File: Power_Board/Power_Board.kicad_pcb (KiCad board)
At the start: 2 copper layers, 70.6 x 70.4 mm, 20 parts, among them J1 Conn_01x10_Female, J2 Conn_01x10_Female, J3 Conn_01x06_Female, J4 Screw_Terminal_01x02, J5 Screw_Terminal_01x02

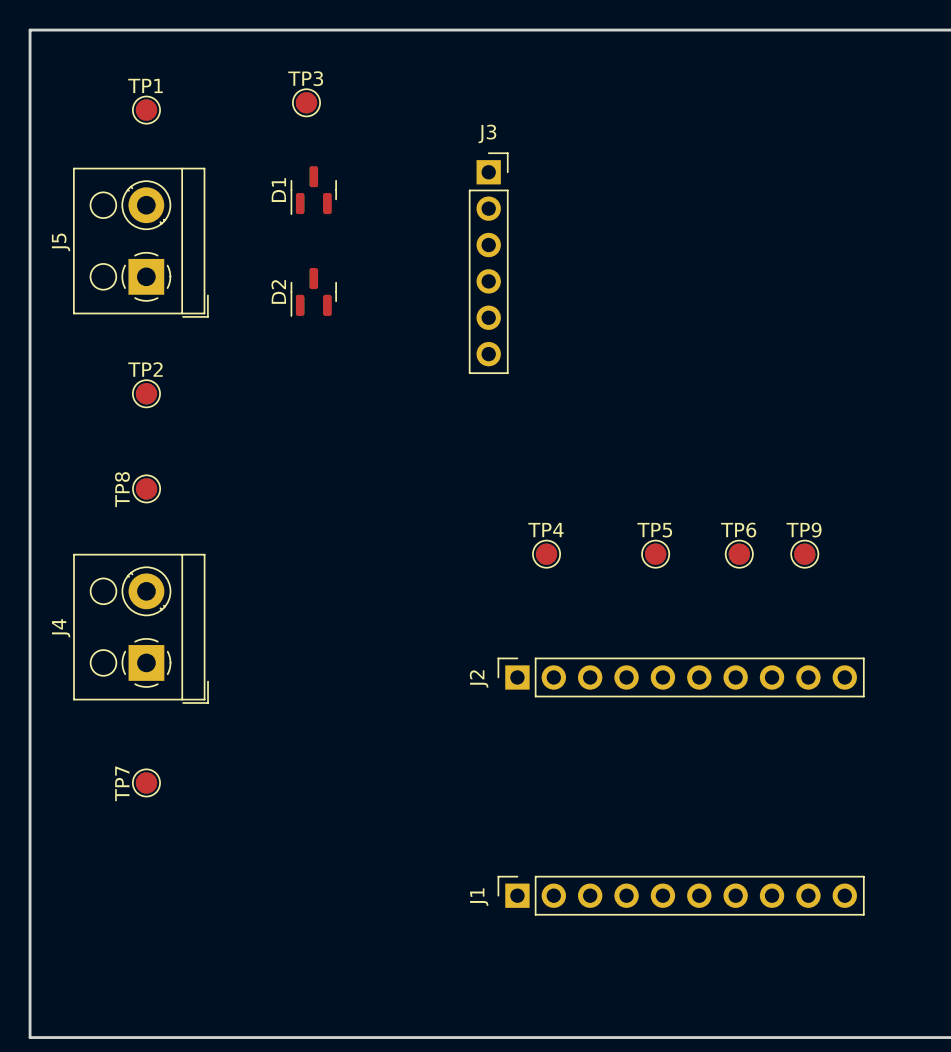
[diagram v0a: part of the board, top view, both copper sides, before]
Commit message: Removed sensor from board
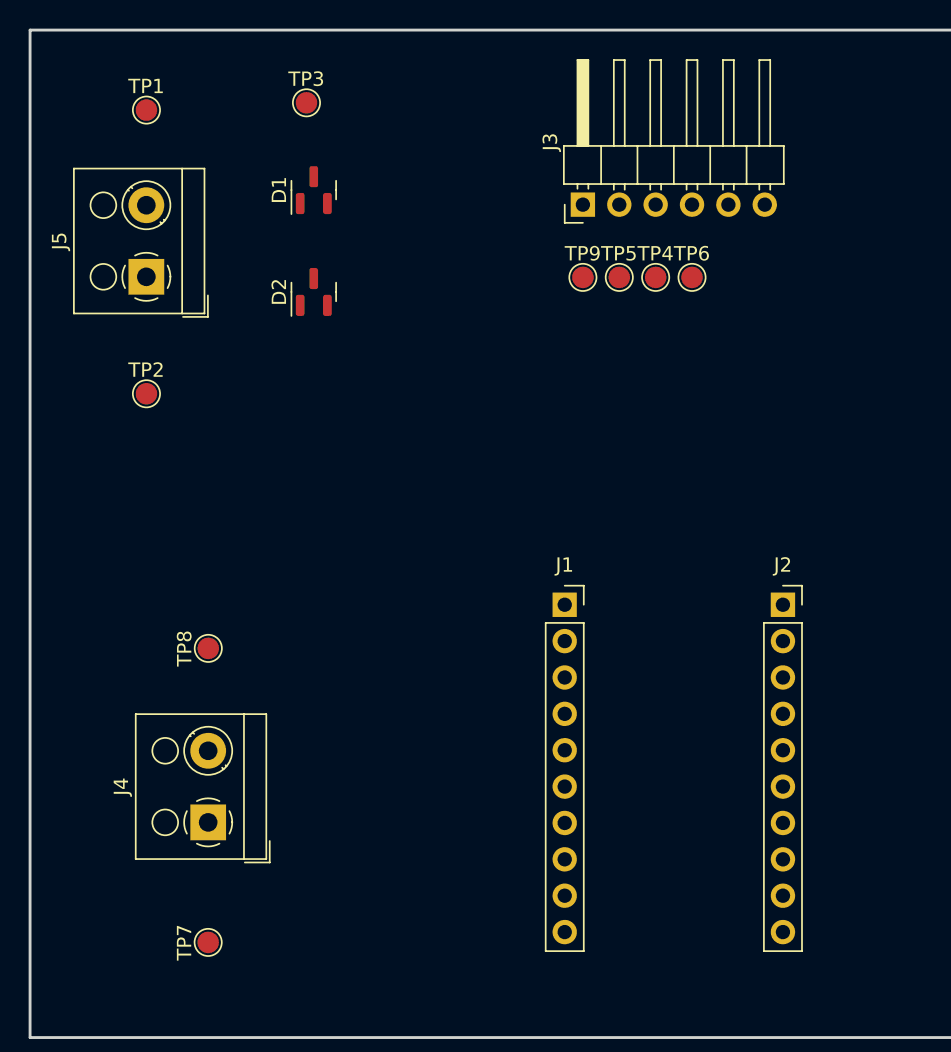
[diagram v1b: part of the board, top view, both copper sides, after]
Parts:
- J3: value Conn_01x06_Female -> Conn_01x06_Male; footprint Connector_PinSocket_2.54mm:PinSocket_1x06_P2.54mm_Vertical -> Connector_PinHeader_2.54mm:PinHeader_1x06_P2.54mm_Horizontal
- TP4: value VDDOUT -> SDA
- TP5: value 1.15 -> VDDOUT
- TP6: value 1.13 -> SCL
- moved TP9 24.8 mm to (138.4, 38.1)
- moved TP4 20.8 mm to (143.5, 38.1)
- moved J1 20.6 mm to (137.2, 61.0), turned to 0 degrees
- moved TP6 19.6 mm to (146.1, 38.1)
- moved TP5 19.5 mm to (141.0, 38.1)
- moved J2 19.2 mm to (152.4, 61.0), turned to 0 degrees
- moved J4 11.9 mm to (112.3, 76.2)
- moved TP7 11.9 mm to (112.3, 84.5)
- moved TP8 11.9 mm to (112.3, 64.0)
- moved J3 6.96 mm to (138.4, 33.0), turned to 90 degrees
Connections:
- J1 pad 1: 0.13 -> SCL
- J2 pad 2: 3V3 -> VDDOUT
- J3 pad 2: 3V3 -> VDDOUT
- J3 pad 3: 1.15 -> 0.15
- J3 pad 4: 1.13 -> SCL
- TP4 pad 1: 3V3 -> 0.15
- TP5 pad 1: 1.15 -> VDDOUT
- TP6 pad 1: 1.13 -> SCL

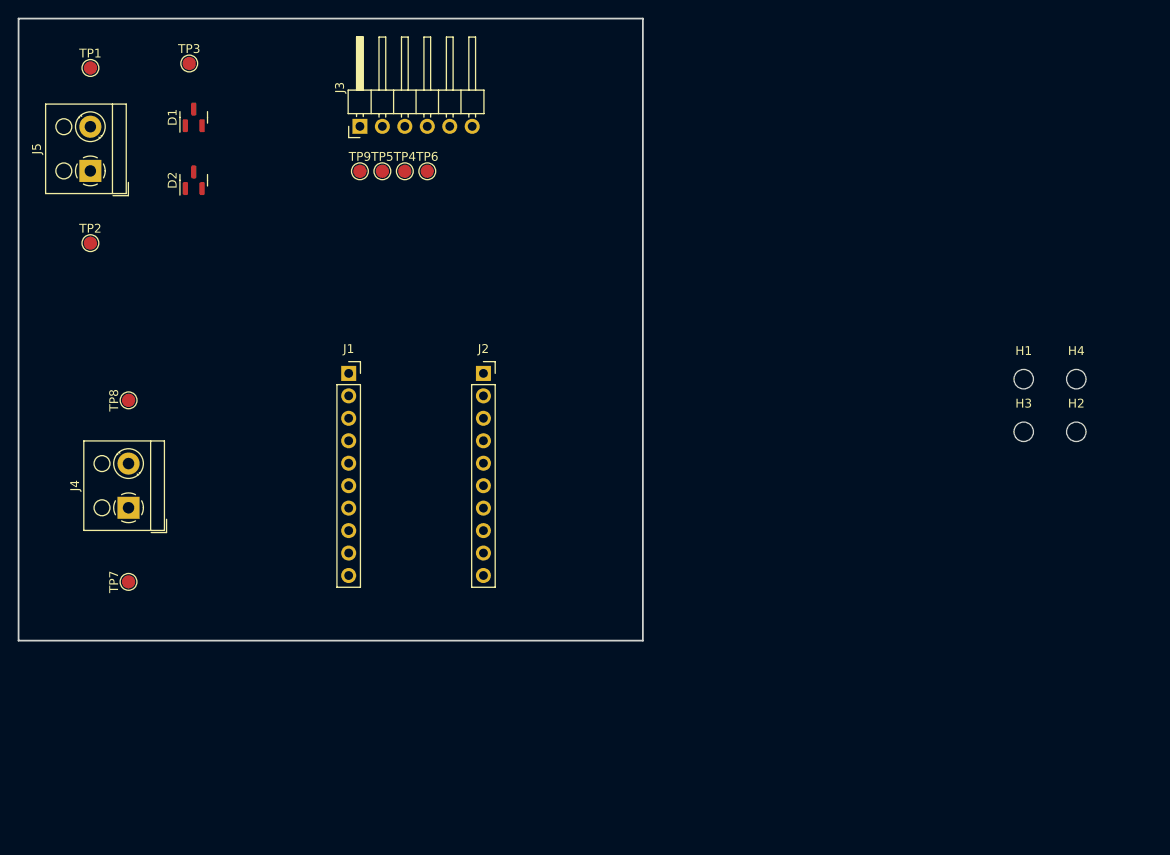
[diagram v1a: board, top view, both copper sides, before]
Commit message: new pcb layout
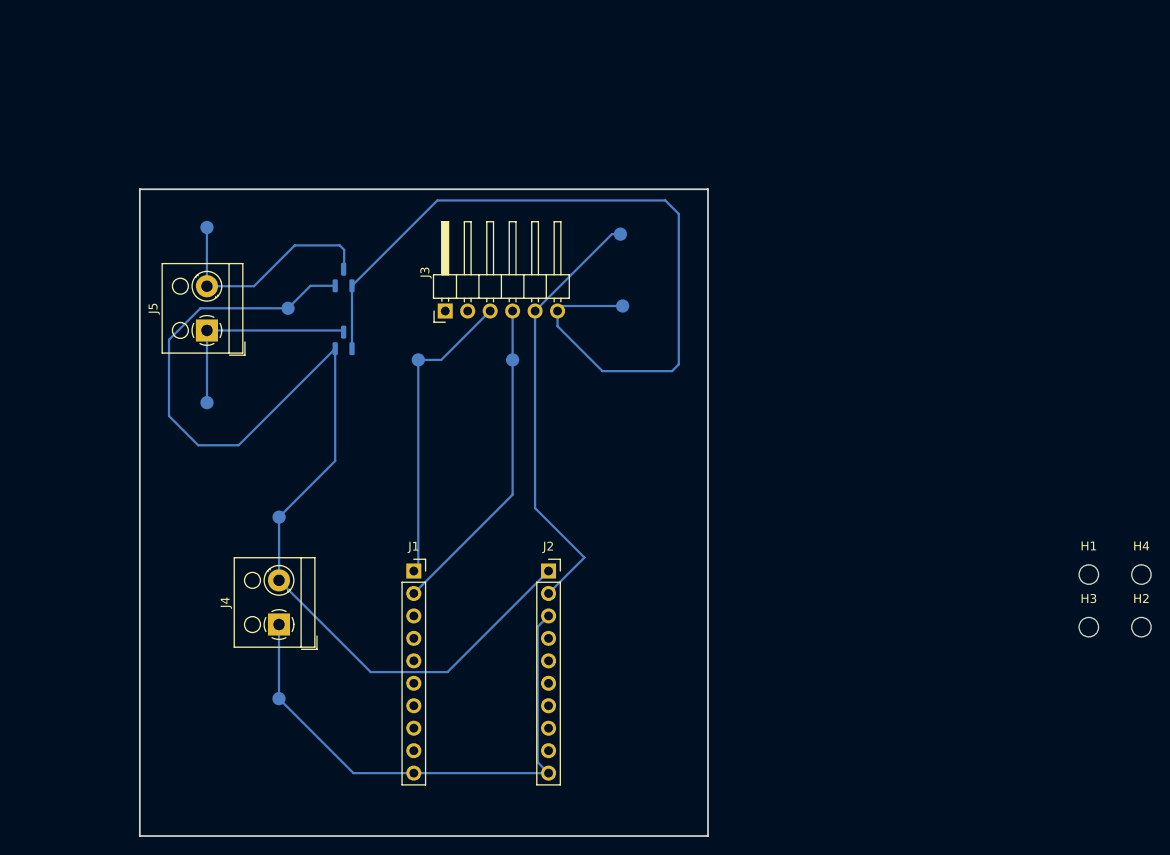
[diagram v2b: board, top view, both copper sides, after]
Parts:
- D1, D2, TP1, TP2, TP3, TP4, TP5, TP6, TP7, TP8, TP9: moved to B.Cu
- moved TP9 33.4 mm to (168.1, 53.3), turned to 180 degrees
- moved TP3 29.9 mm to (130.3, 53.6), turned to 180 degrees
- moved TP5 27.8 mm to (167.9, 45.2), turned to 180 degrees
- moved D1 24.8 mm to (136.6, 50.1)
- moved D2 24.8 mm to (136.6, 57.2)
- moved TP4 24.6 mm to (155.7, 59.4), turned to 180 degrees
- moved J1 23.5 mm to (144.5, 83.3)
- moved J2 23.5 mm to (159.8, 83.3)
- moved H2 23.3 mm to (226.8, 89.7)
- moved H3 23.3 mm to (220.9, 89.7)
- moved H1 23.3 mm to (220.9, 83.7)
- moved H4 23.3 mm to (226.8, 83.7)
- moved J3 23.0 mm to (148.1, 53.9)
- moved J5 22.3 mm to (121.1, 56.1)
- moved TP1 22.3 mm to (121.1, 44.5), turned to 180 degrees
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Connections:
- J1 pad 1: SCL -> 0.13
- J2 pad 2: VDDOUT -> 3V3
- J3 pad 1: GND -> 1V8
- J3 pad 2: VDDOUT -> INT
- J3 pad 3: 0.15 -> 0.13
- J3 pad 4: SCL -> 0.15
- J3 pad 5: INT -> 3V3
- J3 pad 6: 1V8 -> GND
- TP5 pad 1: VDDOUT -> 3V3
- TP6 pad 1: SCL -> 0.13
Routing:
- net GND: track 0.00 -> 152.3 mm
- net VBUS: track 0.00 -> 123.0 mm
- net 3V3: track 0.00 -> 49.2 mm
- net 0.15: track 0.00 -> 36.6 mm
- net 0.13: track 0.00 -> 34.5 mm
- net Net-(D1-Pad3): track 0.00 -> 26.5 mm
- net Net-(D2-Pad3): track 0.00 -> 23.7 mm
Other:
- board size 70.6 x 70.4 mm -> 64.3 x 73.2 mm

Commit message: Added GND plane and rerouted
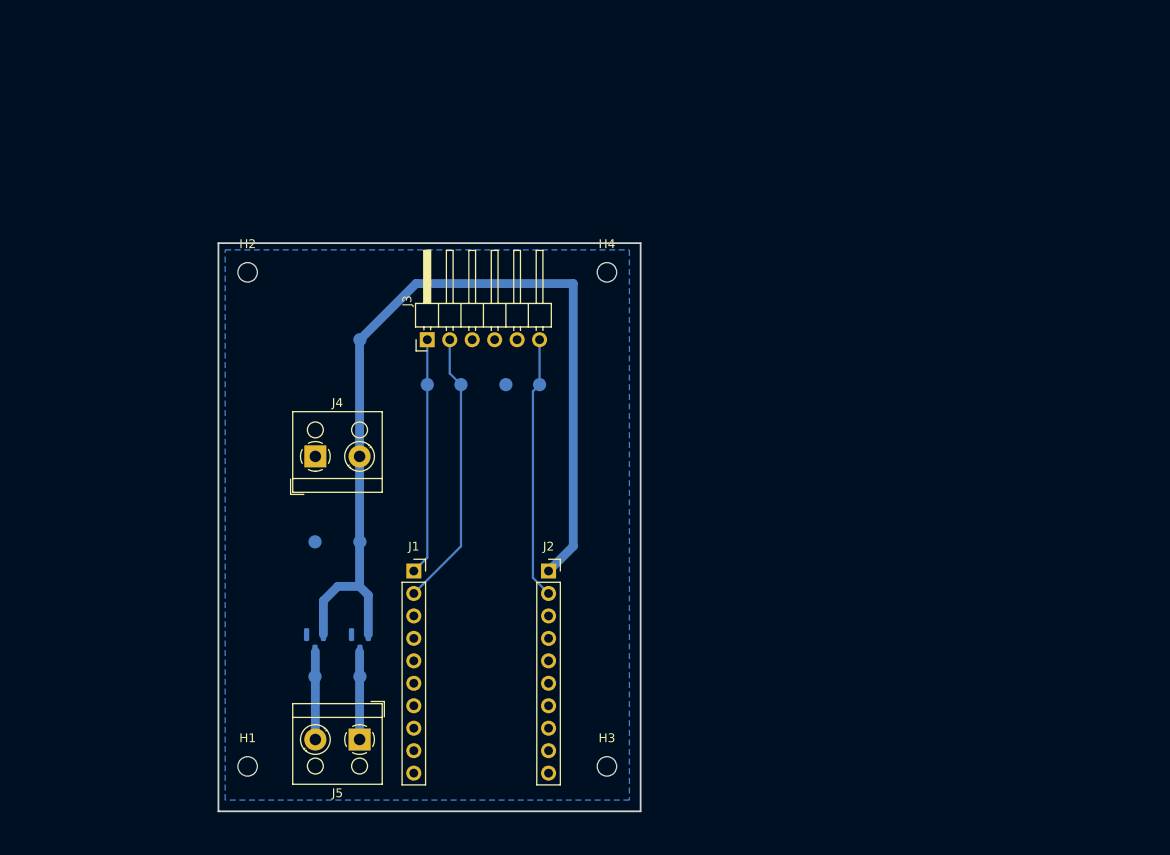
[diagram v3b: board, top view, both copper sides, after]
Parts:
- moved H2 108.8 mm to (125.7, 49.5)
- moved H1 97.6 mm to (125.7, 105.4)
- moved H4 69.4 mm to (166.4, 49.5)
- moved H3 56.7 mm to (166.4, 105.4)
- moved TP1 52.2 mm to (133.3, 95.2)
- moved J5 49.4 mm to (138.4, 102.4), turned to 180 degrees
- moved D1 41.5 mm to (133.3, 91.4), turned to -90 degrees
- moved TP2 35.5 mm to (138.4, 95.2)
- moved D2 34.3 mm to (138.4, 91.4), turned to -90 degrees
- moved TP3 27.6 mm to (138.4, 80.0)
- moved TP8 22.1 mm to (138.4, 57.1)
- moved J4 19.5 mm to (133.4, 70.3), turned to 0 degrees
- moved TP5 19.3 mm to (158.8, 62.2)
- moved TP7 18.2 mm to (133.3, 80.0)
- moved TP9 15.9 mm to (154.9, 62.2)
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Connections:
- J2 pad 2: 3V3 -> VDDOUT
- J3 pad 1: 1V8 -> 0.13
- J3 pad 2: INT -> 0.15
- J3 pad 3: 0.13 -> INT
- J3 pad 4: 0.15 -> 1V8
- J3 pad 5: 3V3 -> GND
- J3 pad 6: GND -> VDDOUT
- TP5 pad 1: 3V3 -> VDDOUT
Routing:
- net GND: track 152.3 -> 0.00 mm
- net 3V3: track 49.2 -> 0.00 mm
- net VDDOUT: track 0.00 -> 29.7 mm
- net VBUS: track 123.0 -> 102.8 mm
- net Net-(D1-Pad3): track 26.5 -> 10.0 mm
- net Net-(D2-Pad3): track 23.7 -> 10.0 mm
- net 0.13: track 34.5 -> 26.8 mm
- net 0.15: track 36.6 -> 31.4 mm
- added copper zone on B.Cu, net GND
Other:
- board size 64.3 x 73.2 mm -> 47.8 x 64.3 mm
